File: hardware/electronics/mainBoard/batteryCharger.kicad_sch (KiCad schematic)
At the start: 63 parts, among them J24 M8AS-02PFFR-SF8001, J25 MUSBRM1C1M0, J26 S2B-PH-SM4-TB, Q1 CSD17581Q3A, Q2 CSD17581Q3A, Q3 CSD17581Q3A, Q4 CSD17581Q3A, Q5 CSD17581Q3A, U21 BQ25798

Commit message: assigned FPs
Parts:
- D15, D16: footprint (none) -> lib_diodes:SOD523
- J24: footprint (none) -> lib_connectors:M8AS-02PFFR-SF8001
- J25: footprint (none) -> lib_connectors:MUSBR-M1C1-XX
- J26: footprint (none) -> lib_connectors:JST-PH-S2B-SM4-TB
- L6: footprint (none) -> lib_passives:WE-XHMI-4030
- Q1, Q2, Q3, Q4, Q5: footprint (none) -> lib_ICs:SON65P300X315X90-8
- U21: footprint (none) -> lib_ICs:QFN40P400X400X100-29
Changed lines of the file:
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@@
 			)
 		)
-		(property "Footprint" ""
+		(property "Footprint" "lib_diodes:SOD523"
 			(at 87.63 81.28 90)
 			(effects
@@
 			)
 		)
-		(property "Footprint" ""
+		(property "Footprint" "lib_ICs:SON65P300X315X90-8"
 			(at 75.565 73.66 90)
 			(effects
@@
 			)
 		)
-		(property "Footprint" ""
+		(property "Footprint" "lib_ICs:SON65P300X315X90-8"
 			(at 167.64 109.855 90)
 			(effects
@@
 			)
 		)
-		(property "Footprint" ""
+		(property "Footprint" "lib_connectors:MUSBR-M1C1-XX"
 			(at 25.4 106.68 0)
 			(effects
@@
 			)
 		)
-		(property "Footprint" ""
+		(property "Footprint" "lib_ICs:QFN40P400X400X100-29"
 			(at 139.7 107.95 0)
 			(effects
@@
 			)
 		)
-		(property "Footprint" ""
+		(property "Footprint" "lib_connectors:JST-PH-S2B-SM4-TB"
 			(at 248.92 146.05 0)
 			(effects
@@
 			)
 		)
-		(property "Footprint" ""
+		(property "Footprint" "lib_passives:WE-XHMI-4030"
 			(at 111.76 110.49 90)
 			(effects
@@
 			)
 		)
-		(property "Footprint" ""
+		(property "Footprint" "lib_ICs:SON65P300X315X90-8"
 			(at 99.695 57.15 90)
 			(effects
@@
 			)
 		)
-		(property "Footprint" ""
+		(property "Footprint" "lib_ICs:SON65P300X315X90-8"
 			(at 99.695 73.66 90)
 			(effects
@@
 			)
 		)
-		(property "Footprint" ""
+		(property "Footprint" "lib_connectors:M8AS-02PFFR-SF8001"
 			(at 25.4 41.91 0)
 			(effects
@@
 			)
 		)
-		(property "Footprint" ""
+		(property "Footprint" "lib_ICs:SON65P300X315X90-8"
 			(at 75.565 57.15 90)
 			(effects
@@
 			)
 		)
-		(property "Footprint" ""
+		(property "Footprint" "lib_diodes:SOD523"
 			(at 87.63 50.8 90)
 			(effects

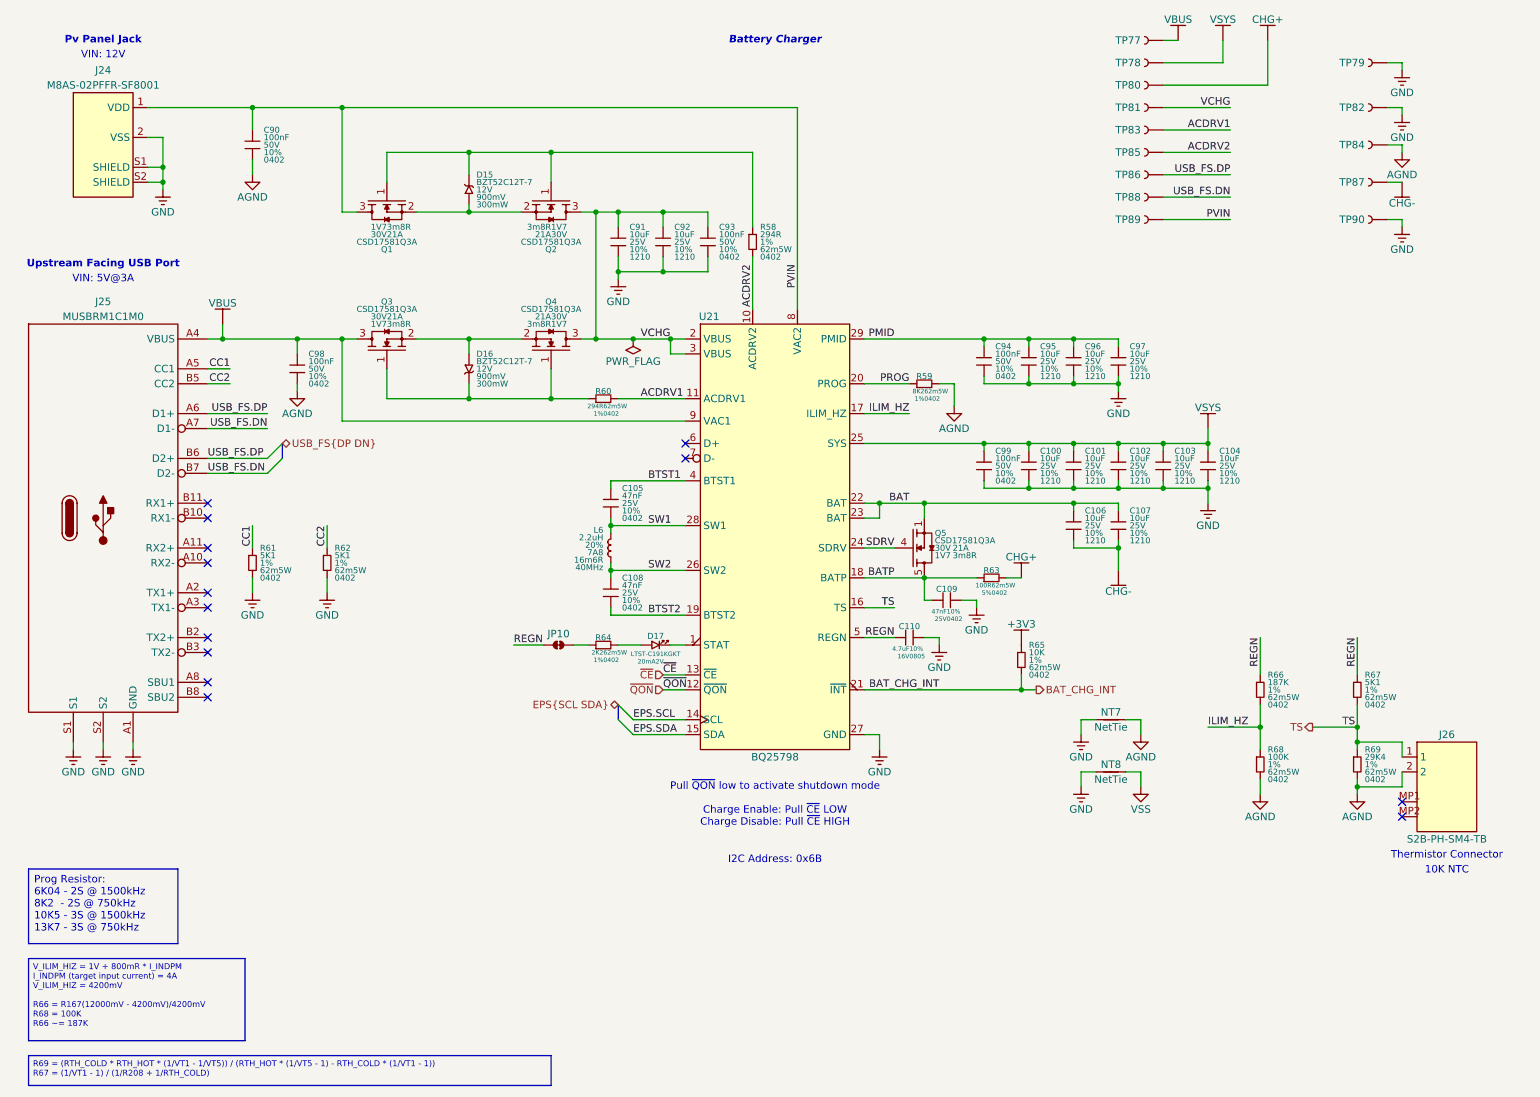
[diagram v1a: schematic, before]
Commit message: assigned footprints
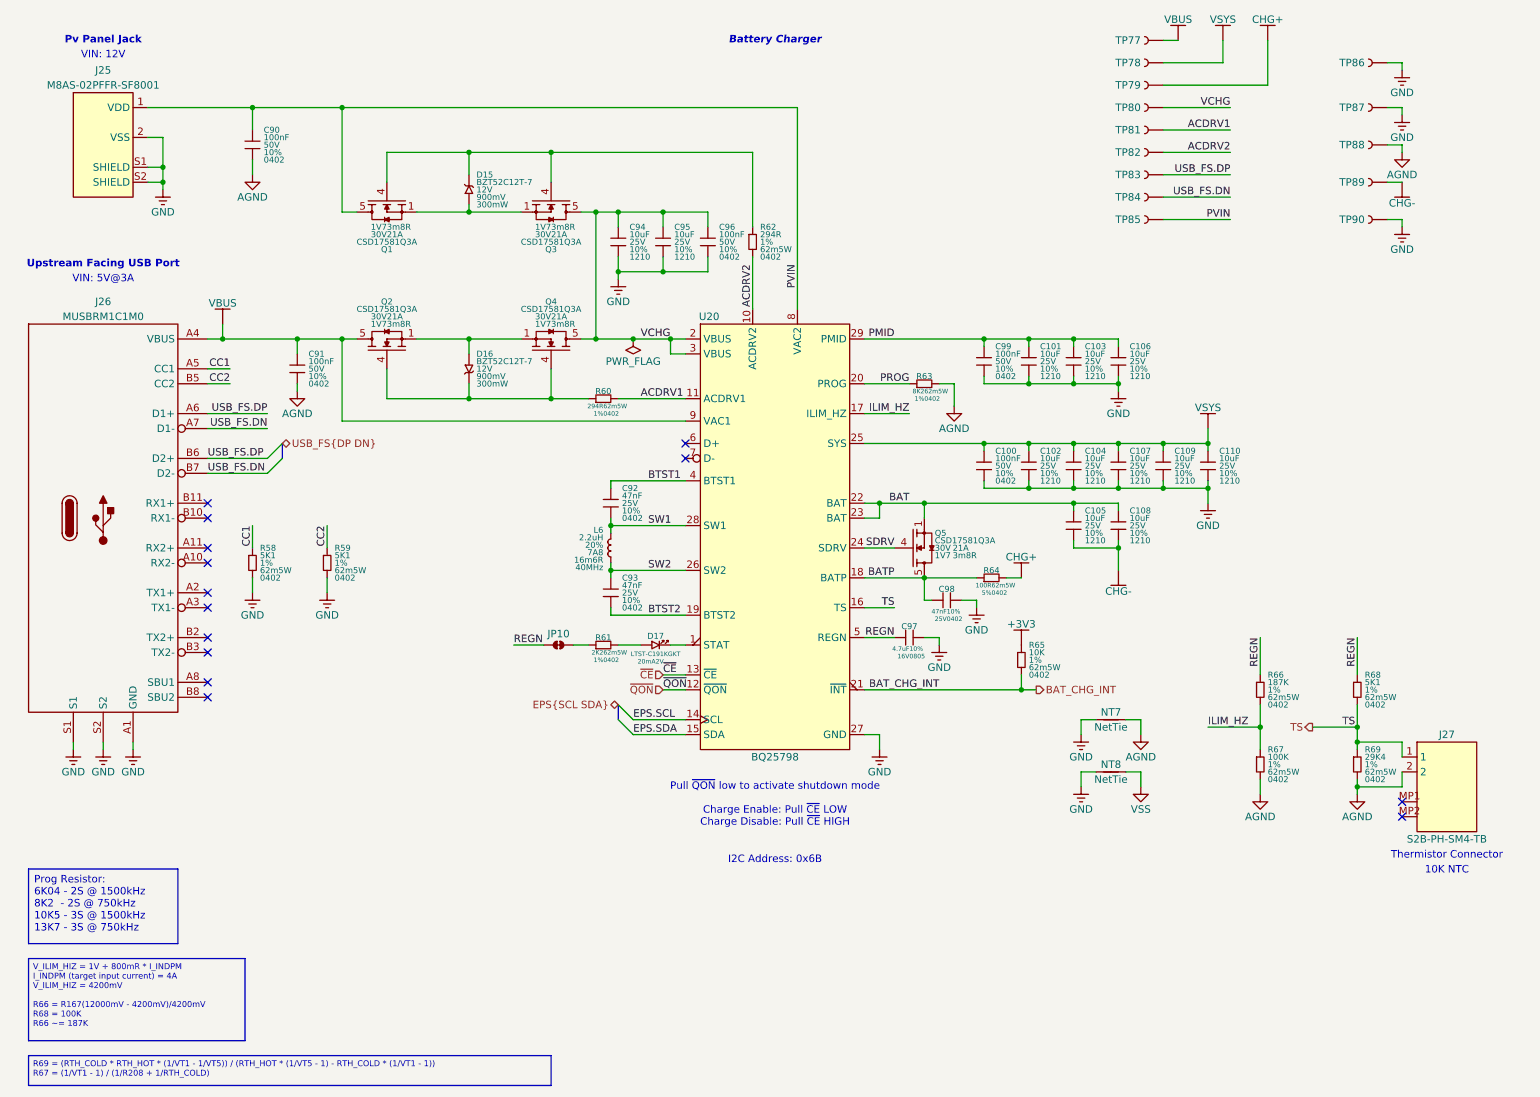
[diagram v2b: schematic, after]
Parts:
- removed Q1, Q2, Q3, Q4: CSD17581Q3A, lib_ICs:SON65P300X315X90-8, symbol lib_sch:NMOS_GSD
- added Q1, Q2, Q3, Q4: CSD17581Q3A, lib_ICs:SON65P300X315X90-8, symbol lib_sch:NMOS_SGD_PWR
- C100: renamed from C99; footprint (none) -> lib_passives:GCM0402
- C101: renamed from C95; footprint (none) -> lib_passives:GRT1210
- C102: renamed from C100; footprint (none) -> lib_passives:GRT1210
- C103: renamed from C96; footprint (none) -> lib_passives:GRT1210
- C104: renamed from C101; footprint (none) -> lib_passives:GRT1210
- C105: renamed from C106; footprint (none) -> lib_passives:GRT1210
- C106: renamed from C97; footprint (none) -> lib_passives:GRT1210
- C107: renamed from C102; footprint (none) -> lib_passives:GRT1210
- C108: renamed from C107; footprint (none) -> lib_passives:GRT1210
- C109: renamed from C103; footprint (none) -> lib_passives:GRT1210
- C110: renamed from C104; footprint (none) -> lib_passives:GRT1210
- C90: footprint (none) -> lib_passives:GCM0402
- C91: renamed from C98; footprint (none) -> lib_passives:GCM0402
- C92: renamed from C105; footprint (none) -> lib_passives:GCM0402
- C93: renamed from C108; footprint (none) -> lib_passives:GCM0402
- C94: renamed from C91; footprint (none) -> lib_passives:GRT1210
- C95: renamed from C92; footprint (none) -> lib_passives:GRT1210
- C96: renamed from C93; footprint (none) -> lib_passives:GCM0402
- C97: renamed from C110; footprint (none) -> lib_passives:GCM0805
- C98: renamed from C109; footprint (none) -> lib_passives:GCM0402
- C99: renamed from C94; footprint (none) -> lib_passives:GCM0402
- D17: footprint (none) -> lib_diodes:LTST-0603
- JP10: footprint (none) -> lib_misc:SolderJumper-2_P1.3mm_Bridged_RoundedPad1.0x1.5mm
- NT7, NT8: footprint (none) -> lib_misc:NetTie-2_SMD_Pad2.0mm
- R58: renamed from R61; footprint (none) -> lib_passives:CRCW0402
- R59: renamed from R62; footprint (none) -> lib_passives:CRCW0402
- R60, R65, R66, R69: footprint (none) -> lib_passives:CRCW0402
- R61: renamed from R64; footprint (none) -> lib_passives:CRCW0402
- R62: renamed from R58; footprint (none) -> lib_passives:CRCW0402
- R63: renamed from R59; footprint (none) -> lib_passives:CRCW0402
- R64: renamed from R63; footprint (none) -> lib_passives:CRCW0402
- R67: renamed from R68; footprint (none) -> lib_passives:CRCW0402
- R68: renamed from R67; footprint (none) -> lib_passives:CRCW0402
- TP77, TP78: footprint (none) -> lib_misc:TP_2mm
- TP79: renamed from TP80; footprint (none) -> lib_misc:TP_2mm
- TP80: renamed from TP81; footprint (none) -> lib_misc:TP_2mm
- TP81: renamed from TP83; footprint (none) -> lib_misc:TP_2mm
- TP82: renamed from TP85; footprint (none) -> lib_misc:TP_2mm
- TP83: renamed from TP86; footprint (none) -> lib_misc:TP_2mm
- TP84: renamed from TP88; footprint (none) -> lib_misc:TP_2mm
- TP85: renamed from TP89; footprint (none) -> lib_misc:TP_2mm
- TP86: renamed from TP79; footprint (none) -> lib_misc:TP_RCW
- TP87: renamed from TP82; footprint (none) -> lib_misc:TP_RCW
- TP88: renamed from TP84; footprint (none) -> lib_misc:TP_RCW
- TP89: renamed from TP87; footprint (none) -> lib_misc:TP_RCW
- TP90: footprint (none) -> lib_misc:TP_RCW
- renumbered J24 to J25, J25 to J26, J26 to J27, U21 to U20
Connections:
- net BATP: now also Q5.9
- net GND: now also J26.G1 (GND), J26.G2 (GND), J26.G3 (GND), J26.G4 (GND), J26.G5 (GND), J26.G6 (GND)
- net PVIN: now also Q1.5, Q1.6, Q1.7, Q1.8, Q1.9
- net VBUS: now also Q2.5, Q2.6, Q2.7, Q2.8, Q2.9
- net VCHG: now also Q3.5, Q3.6, Q3.7, Q3.8, Q3.9, Q4.5, Q4.6, Q4.7, Q4.8, Q4.9
- net at D16.2, R60.1: now also Q2.4, Q4.4
- net at D16.1: now also Q2.1, Q2.2, Q2.3, Q4.1, Q4.2, Q4.3
- net at D15.2, R62.1: now also Q1.4, Q3.4
- net at D15.1: now also Q1.1, Q1.2, Q1.3, Q3.1, Q3.2, Q3.3

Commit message: updated ref designators
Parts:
- Q2: renamed from Q3; MPN Texas Instruments -> CSD17581Q3A
- renumbered C102 to C100, C104 to C101, C107 to C102, C109 to C103, C110 to C104, C92 to C105, C105 to C106, C108 to C107, C93 to C108, C98 to C109, C97 to C110, C94 to C91, C95 to C92, C96 to C93, C99 to C94, C101 to C95, C103 to C96, C106 to C97, C91 to C98, C100 to C99, Q2 to Q3, R62 to R61, R63 to R62, R60 to R63, R58 to R64, R59 to R65, R64 to R66, R61 to R67, R65 to R68, R66 to R69, R68 to R70, R67 to R71, R69 to R72, TP86 to TP79, TP79 to TP80, TP80 to TP81, TP87 to TP82, TP81 to TP83, TP88 to TP84, TP82 to TP85, TP83 to TP86, TP89 to TP87, TP84 to TP88, TP85 to TP89

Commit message: fixed sch
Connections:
- net BATP: no longer Q5.5, Q5.6, Q5.7, Q5.8, Q5.9
- net CHG+: now also Q5.5, Q5.6, Q5.7, Q5.8, Q5.9
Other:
- moved on the sheet: C109, Q5, R66

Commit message: minor changes
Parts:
- added D5: PTVS13VS1UR, lib_diodes:SOD123W, symbol DS-Diodes:D_TVS_single
- added D6, D8: ESD321DYAR, lib_diodes:SOD523, symbol DS-Diodes:D_TVS_single
- added D9: TPD1E05U06-Q1, lib_diodes:SON2P65_100X60X50L50X25N, symbol DS-Diodes:D_TVS_single
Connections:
- net GND: now also D5.2, D6.2, D8.2, D9.2
- net PVIN: now also D5.1
- net USB_FS.DN: now also D8.1
- net USB_FS.DP: now also D6.1
- net VBUS: now also D9.1
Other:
- moved on the sheet: C90, C98, Q3, R64, R65

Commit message: redefined symbol refs
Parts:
- renumbered C99 to C100, C100 to C101, C101 to C102, C102 to C103, C103 to C104, C104 to C105, C105 to C106, C106 to C107, C107 to C108, C108 to C109, C109 to C110, C110 to C111, C90 to C91, C91 to C92, C92 to C93, C93 to C94, C94 to C95, C95 to C96, C96 to C97, C97 to C98, C98 to C99, D15 to D10, D9 to D11, D16 to D12, D6 to D13, D8 to D14, D17 to D15, D5 to D9, JP10 to JP4, R61 to R55, R62 to R56, R63 to R57, R66 to R58, R64 to R59, R65 to R60, R67 to R61, R68 to R62, R69 to R63, R70 to R64, R71 to R65, R72 to R66

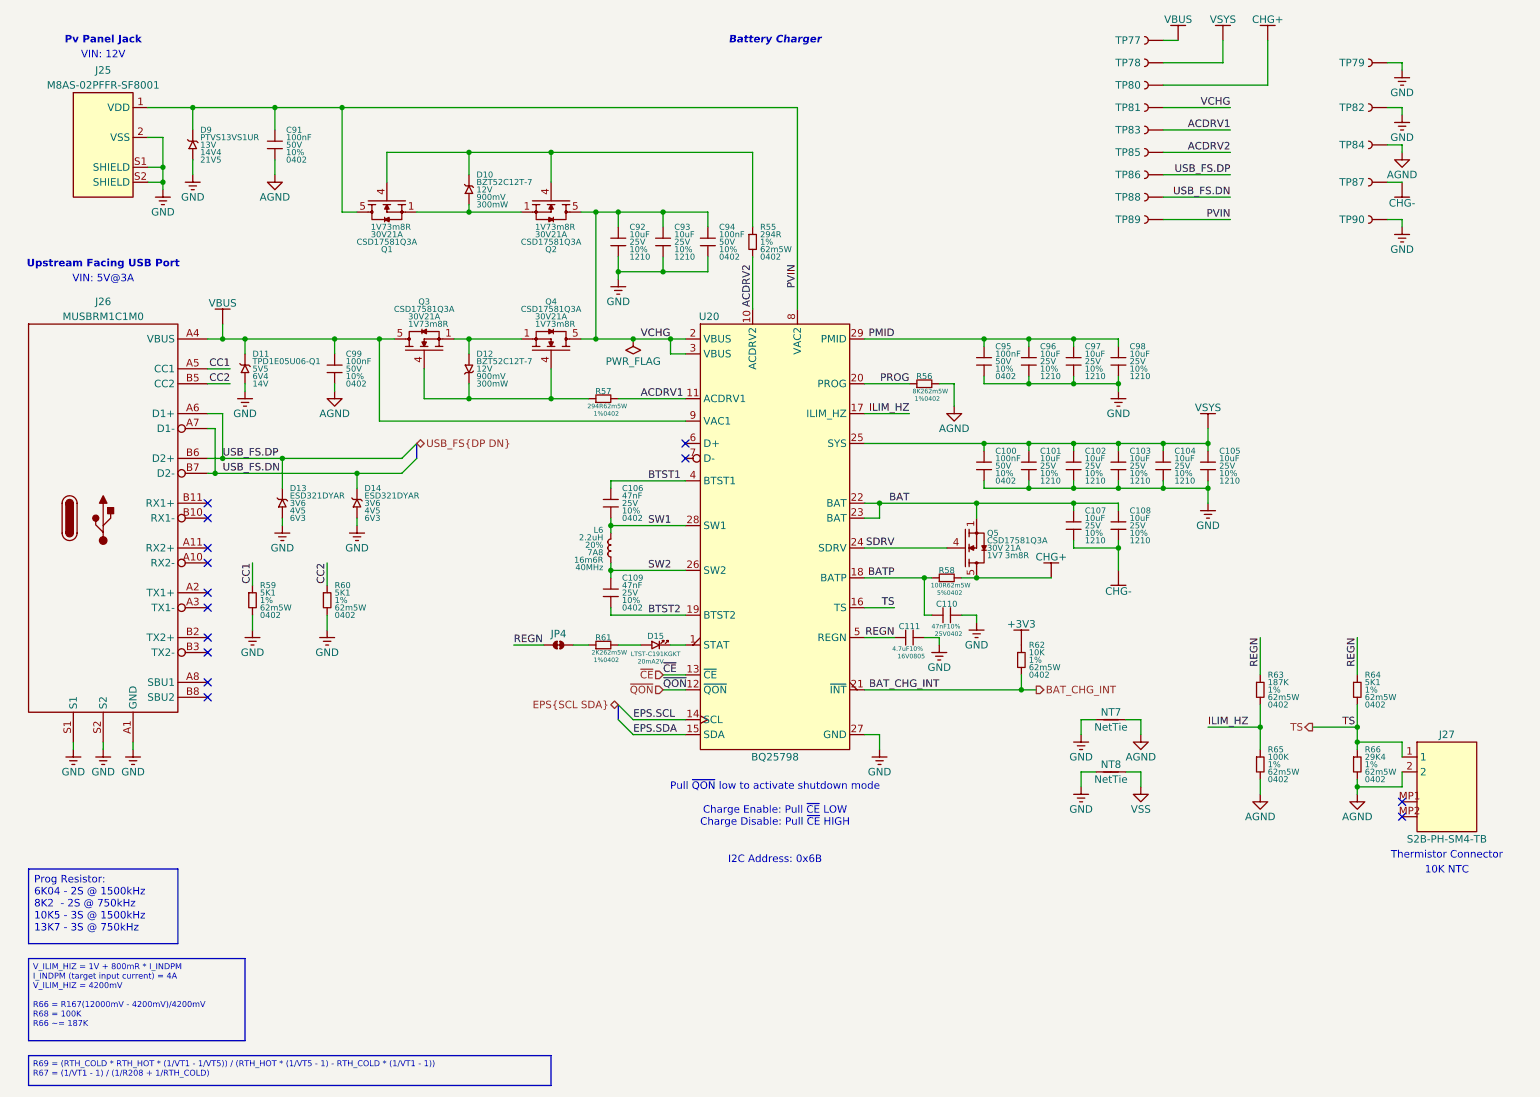
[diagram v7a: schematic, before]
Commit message: moved USB port to USB hub page
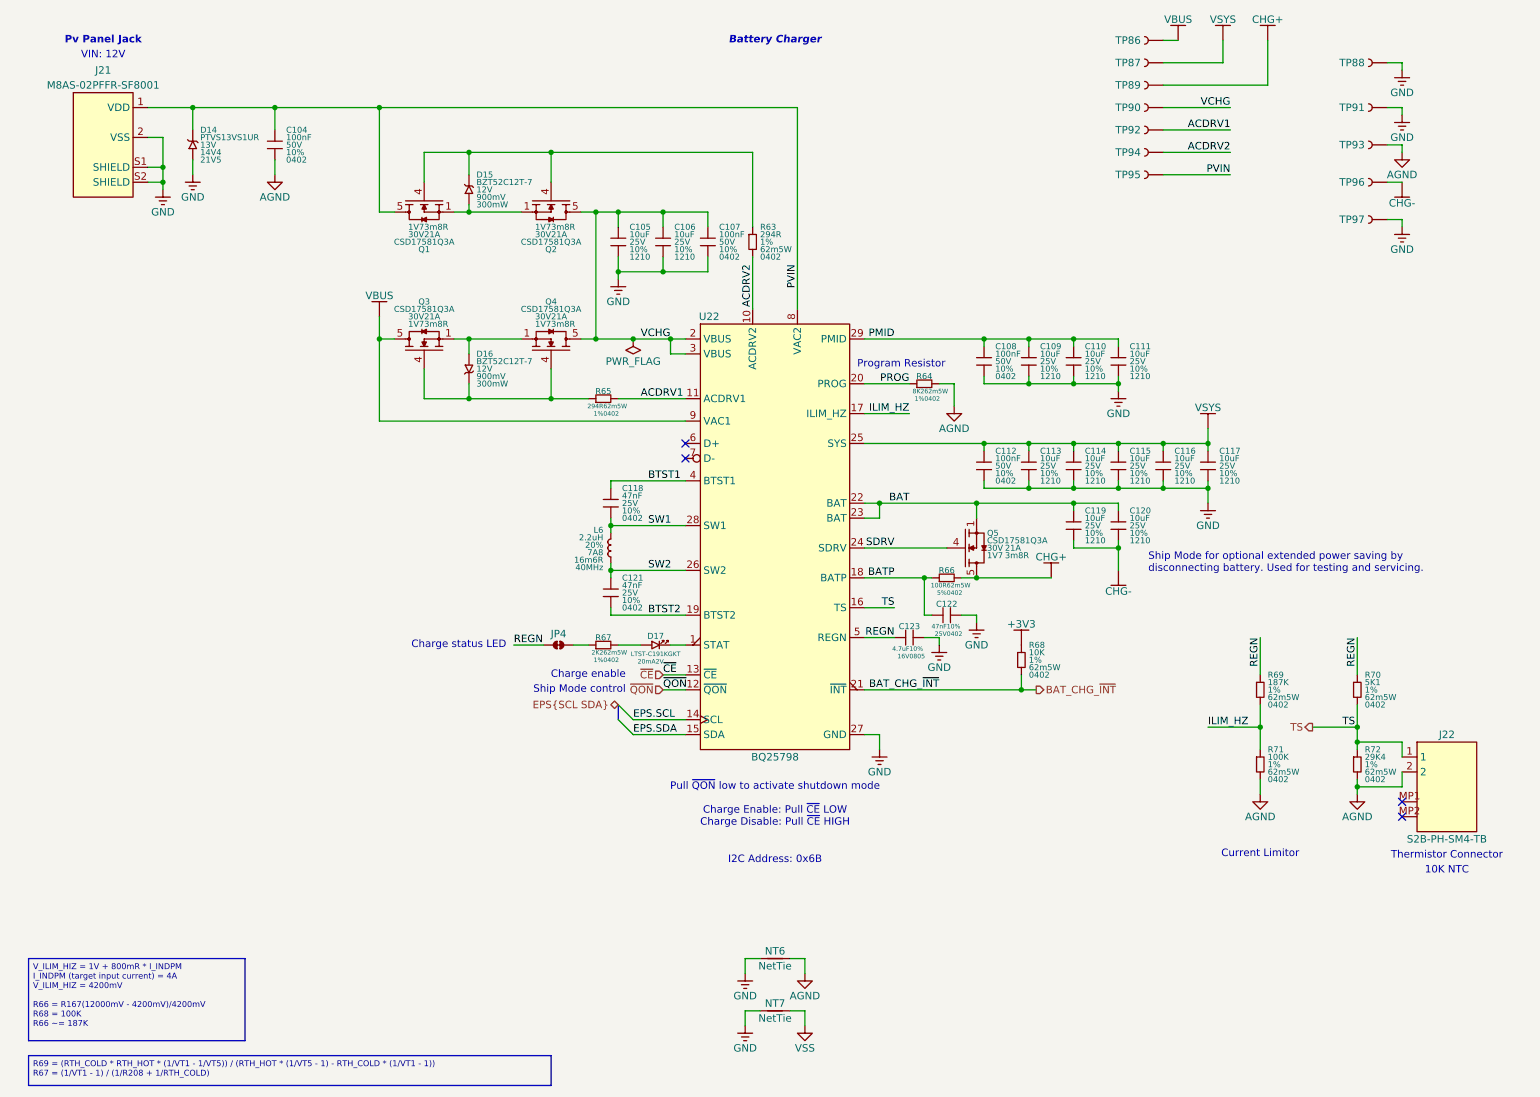
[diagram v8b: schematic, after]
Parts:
- removed C99: 100nF, lib_passives:GCM0402, symbol lib_sch:C
- removed D11: TPD1E05U06-Q1, lib_diodes:SON2P65_100X60X50L50X25N, symbol DS-Diodes:D_TVS_single
- removed D13, D14: ESD321DYAR, lib_diodes:SOD523, symbol DS-Diodes:D_TVS_single
- removed J26: MUSBRM1C1M0, lib_connectors:MUSBR-M1C1-XX, symbol lib_sch:USB_C_Receptacle_24P
- removed R59, R60: 5K1, lib_passives:CRCW0402, symbol lib_sch:R
- removed TP86, TP88: ~, lib_misc:TP_2mm, symbol lib_sch:Testpoint
- renumbered C91 to C104, C92 to C105, C93 to C106, C94 to C107, C95 to C108, C96 to C109, C97 to C110, C98 to C111, C100 to C112, C101 to C113, C102 to C114, C103 to C115, C104 to C116, C105 to C117, C106 to C118, C107 to C119, C108 to C120, C109 to C121, C110 to C122, C111 to C123, D9 to D14, D10 to D15, D12 to D16, D15 to D17, J25 to J21, J27 to J22, NT7 to NT6, NT8 to NT7, R55 to R63, R56 to R64, R57 to R65, R58 to R66, R61 to R67, R62 to R68, R63 to R69, R64 to R70, R65 to R71, R66 to R72, TP77 to TP86, TP78 to TP87, TP79 to TP88, TP80 to TP89, TP81 to TP90, TP82 to TP91, TP83 to TP92, TP84 to TP93, TP85 to TP94, TP89 to TP95, TP87 to TP96, TP90 to TP97, U20 to U22
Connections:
- net BAT_CHG_INT renamed BAT_CHG_~{INT}
- no-connect marks 14 -> 4
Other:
- note added: "Charge enable"
- note added: "Charge status LED"
- note added: "Current Limitor"
- note added: "Program Resistor"
- note added: "Ship Mode control"
- note added: "Ship Mode for optional extended power saving by disconnecting battery. Used for testing and servicing."
- note removed: "Upstream Facing USB Port"
- note removed: "VIN: 5V@3A"
- moved on the sheet: NT6, NT7, Q1, TP95
